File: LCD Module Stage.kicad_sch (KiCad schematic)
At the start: 8 parts, among them Q4 AO3400A, U8 1.8inch LCD Module

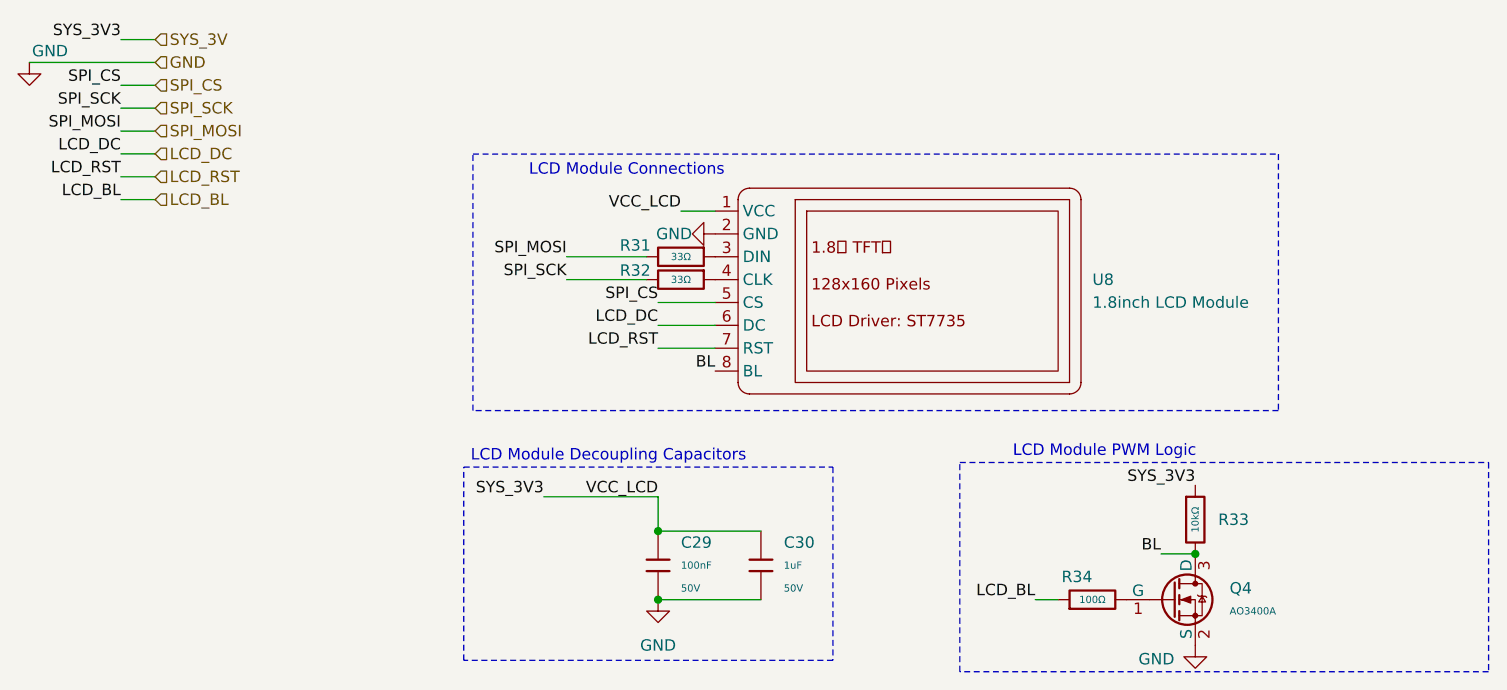
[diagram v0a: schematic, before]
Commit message: - Added Hysteresis resistor on TLV431BSN1T1G - Lowered TLV431BSN1T1G impedance values for resistors on the voltage divider
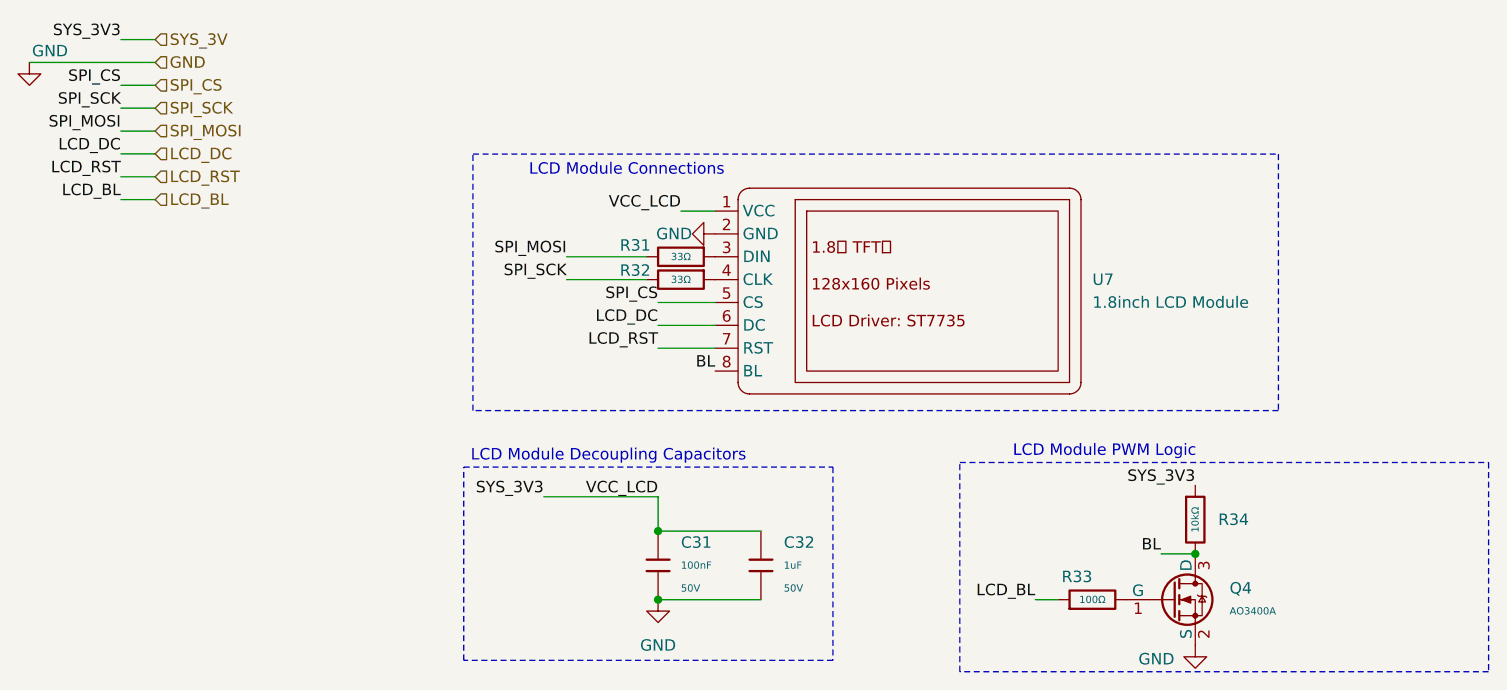
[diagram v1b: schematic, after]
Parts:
- U7: renamed from U8; footprint (none) -> LED_THT_Custom:Waveshare 1.8inch LCD Module
- renumbered C29 to C31, C30 to C32, R34 to R33, R33 to R34
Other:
- company: Yaniv Lieberman -> (none)
- title: (none) -> Integrated Si5351A Module - LCD Module Stage
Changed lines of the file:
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@@
 	(paper "A4")
 	(title_block
+		(title "Integrated Si5351A Module - LCD Module Stage")
 		(date "2026-02-09")
 		(rev "REV1")
-		(company "Yaniv Lieberman")
 	)
 	(rectangle
@@
 		(dnp no)
 		(fields_autoplaced yes)
-		(property "Reference" "R33"
+		(property "Reference" "R34"
 			(at 146.05 71.1199 0)
 			(effects
@@
 			(project ""
 				(path "/5effc93d-4636-458a-a65b-e63d3c617be7/7c71b3d3-cbc7-45da-8155-d18d07019bfb"
-					(reference "R33")
+					(reference "R34")
 					(unit 1)
 				)
@@
 		(dnp no)
 		(fields_autoplaced yes)
-		(property "Reference" "#PWR065"
+		(property "Reference" "#PWR066"
 			(at 83.82 86.36 0)
 			(effects
@@
 			(project ""
 				(path "/5effc93d-4636-458a-a65b-e63d3c617be7/7c71b3d3-cbc7-45da-8155-d18d07019bfb"
-					(reference "#PWR065")
+					(reference "#PWR066")
 					(unit 1)
 				)
@@
 		(dnp no)
 		(fields_autoplaced yes)
-		(property "Reference" "U8"
+		(property "Reference" "U7"
 			(at 132.08 44.4499 0)
 			(effects
@@
 			)
 		)
-		(property "Footprint" ""
+		(property "Footprint" "LED_THT_Custom:Waveshare 1.8inch LCD Module"
 			(at 114.3 45.72 0)
 			(effects
@@
 			(project "Integrate Si5351A Module"
 				(path "/5effc93d-4636-458a-a65b-e63d3c617be7/7c71b3d3-cbc7-45da-8155-d18d07019bfb"
-					(reference "U8")
+					(reference "U7")
 					(unit 1)
 				)
@@
 		(dnp no)
 		(fields_autoplaced yes)
-		(property "Reference" "C30"
+		(property "Reference" "C32"
 			(at 97.79 73.6599 0)
 			(effects
@@
 			(project ""
 				(path "/5effc93d-4636-458a-a65b-e63d3c617be7/7c71b3d3-cbc7-45da-8155-d18d07019bfb"
-					(reference "C30")
+					(reference "C32")
 					(unit 1)
 				)
@@
 		(dnp no)
 		(fields_autoplaced yes)
-		(property "Reference" "C29"
+		(property "Reference" "C31"
 			(at 86.36 73.6599 0)
 			(effects
@@
 			(project ""
 				(path "/5effc93d-4636-458a-a65b-e63d3c617be7/7c71b3d3-cbc7-45da-8155-d18d07019bfb"
-					(reference "C29")
+					(reference "C31")
 					(unit 1)
 				)
@@
 		(on_board yes)
 		(dnp no)
-		(property "Reference" "#PWR062"
+		(property "Reference" "#PWR065"
 			(at 13.97 26.67 0)
 			(effects
@@
 			(project ""
 				(path "/5effc93d-4636-458a-a65b-e63d3c617be7/7c71b3d3-cbc7-45da-8155-d18d07019bfb"
-					(reference "#PWR062")
+					(reference "#PWR065")
 					(unit 1)
 				)
@@
 		(on_board yes)
 		(dnp no)
-		(property "Reference" "#PWR064"
+		(property "Reference" "#PWR068"
 			(at 143.51 91.44 0)
 			(effects
@@
 			(project "Integrate Si5351A Module"
 				(path "/5effc93d-4636-458a-a65b-e63d3c617be7/7c71b3d3-cbc7-45da-8155-d18d07019bfb"
-					(reference "#PWR064")
+					(reference "#PWR068")
 					(unit 1)
 				)
@@
 		(on_board yes)
 		(dnp no)
-		(property "Reference" "R34"
+		(property "Reference" "R33"
 			(at 132.0799 77.47 90)
 			(effects
@@
 			(project ""
 				(path "/5effc93d-4636-458a-a65b-e63d3c617be7/7c71b3d3-cbc7-45da-8155-d18d07019bfb"
-					(reference "R34")
+					(reference "R33")
 					(unit 1)
 				)
@@
 		(on_board yes)
 		(dnp no)
-		(property "Reference" "#PWR063"
+		(property "Reference" "#PWR067"
 			(at 83.82 39.37 0)
 			(effects
@@
 			(project "Integrate Si5351A Module"
 				(path "/5effc93d-4636-458a-a65b-e63d3c617be7/7c71b3d3-cbc7-45da-8155-d18d07019bfb"
-					(reference "#PWR063")
+					(reference "#PWR067")
 					(unit 1)
 				)
